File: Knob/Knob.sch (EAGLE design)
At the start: 17 parts, among them SW1 TopUp EC12PLRGBSDVBF-D, U2 ATTINY841

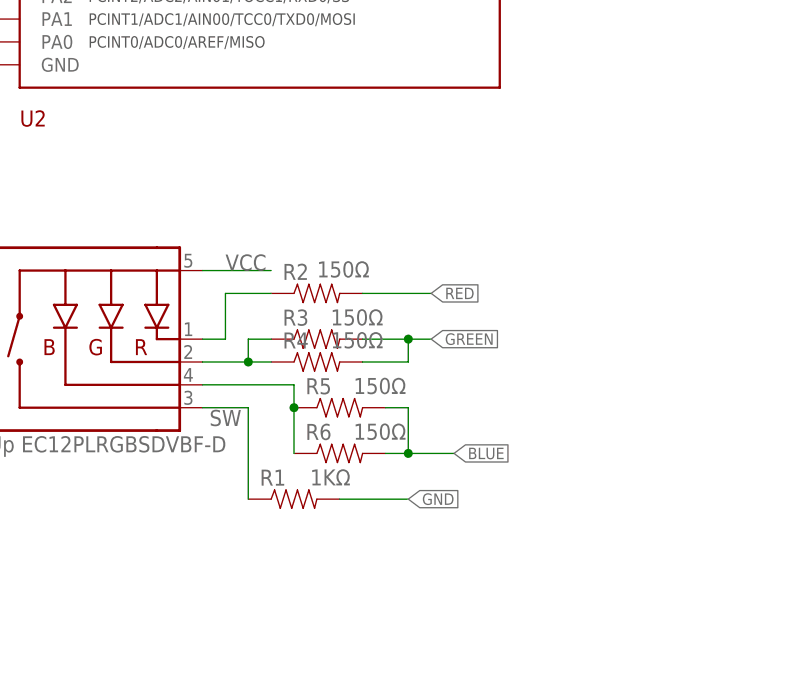
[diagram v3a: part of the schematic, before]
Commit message: Added parallel resistor on red channel for better white balance. Moved status LED to opposite side of the board next to logo Updated to new 0603 footprint.
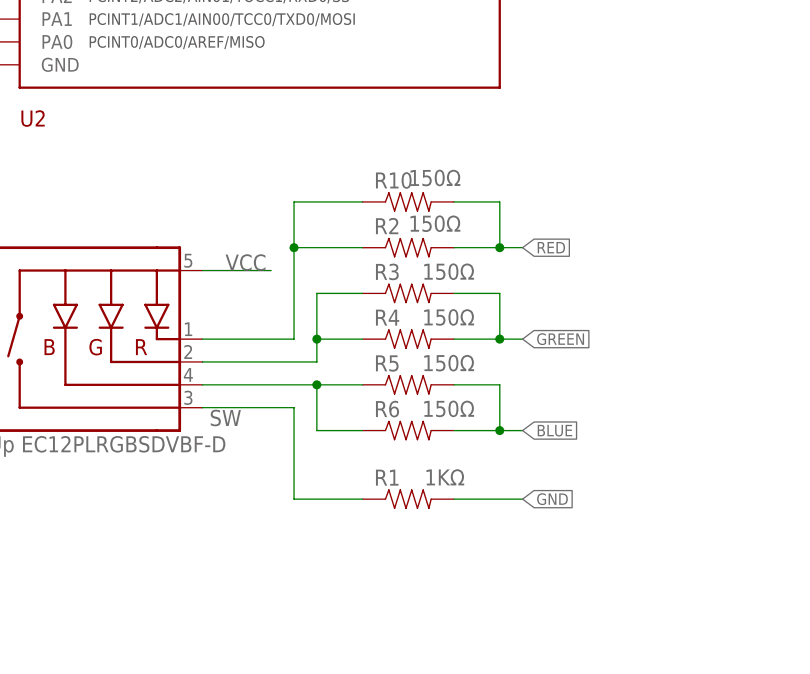
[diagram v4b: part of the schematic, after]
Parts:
- added R10: 150Ω, Modulo:RESISTOR-150Ω
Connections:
- net N$4: now also R10.1
- net RED: now also R10.2
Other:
- moved on the sheet: R1, R2, R3, R4, R5, R6
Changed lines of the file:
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@@
 <part name="R8" library="Modulo" deviceset="RESISTOR" device="-150Ω" value="150Ω"/>
 <part name="R9" library="Modulo" deviceset="RESISTOR" device="-150Ω" value="150Ω"/>
+<part name="R10" library="Modulo" deviceset="RESISTOR" device="-150Ω" value="150Ω"/>
 </parts>
 <sheets>
@@
 <attribute name="PARTNUM" x="63.5" y="73.66" size="1.778" layer="96" display="off"/>
 </instance>
-<instance part="R2" gate="G$1" x="91.44" y="78.74" smashed="yes">
-<attribute name="NAME" x="87.63" y="80.2386" size="1.778" layer="95"/>
-<attribute name="VALUE" x="91.44" y="80.518" size="1.778" layer="96"/>
-</instance>
-<instance part="R3" gate="G$1" x="91.44" y="73.66" smashed="yes">
-<attribute name="NAME" x="87.63" y="75.1586" size="1.778" layer="95"/>
-<attribute name="VALUE" x="92.964" y="75.184" size="1.778" layer="96"/>
-</instance>
-<instance part="R6" gate="G$1" x="93.98" y="60.96" smashed="yes">
-<attribute name="NAME" x="90.17" y="62.4586" size="1.778" layer="95"/>
-<attribute name="VALUE" x="95.504" y="62.484" size="1.778" layer="96"/>
-</instance>
-<instance part="R1" gate="G$1" x="88.9" y="55.88" smashed="yes">
-<attribute name="NAME" x="85.09" y="57.3786" size="1.778" layer="95"/>
-<attribute name="VALUE" x="90.678" y="57.404" size="1.778" layer="96"/>
+<instance part="R2" gate="G$1" x="101.6" y="83.82" smashed="yes">
+<attribute name="NAME" x="97.79" y="85.3186" size="1.778" layer="95"/>
+<attribute name="VALUE" x="101.6" y="85.598" size="1.778" layer="96"/>
+</instance>
+<instance part="R3" gate="G$1" x="101.6" y="78.74" smashed="yes">
+<attribute name="NAME" x="97.79" y="80.2386" size="1.778" layer="95"/>
+<attribute name="VALUE" x="103.124" y="80.264" size="1.778" layer="96"/>
+</instance>
+<instance part="R6" gate="G$1" x="101.6" y="63.5" smashed="yes">
+<attribute name="NAME" x="97.79" y="64.9986" size="1.778" layer="95"/>
+<attribute name="VALUE" x="103.124" y="65.024" size="1.778" layer="96"/>
+</instance>
+<instance part="R1" gate="G$1" x="101.6" y="55.88" smashed="yes">
+<attribute name="NAME" x="97.79" y="57.3786" size="1.778" layer="95"/>
+<attribute name="VALUE" x="103.378" y="57.404" size="1.778" layer="96"/>
 </instance>
 <instance part="FRAME1" gate="G$1" x="0" y="0">
@@
 <instance part="F1" gate="G$1" x="165.1" y="45.72"/>
 <instance part="F2" gate="G$1" x="190.5" y="45.72"/>
-<instance part="R5" gate="G$1" x="93.98" y="66.04" smashed="yes">
-<attribute name="NAME" x="90.17" y="67.5386" size="1.778" layer="95"/>
-<attribute name="VALUE" x="95.504" y="67.564" size="1.778" layer="96"/>
-</instance>
-<instance part="R4" gate="G$1" x="91.44" y="71.12" smashed="yes">
-<attribute name="NAME" x="87.63" y="72.6186" size="1.778" layer="95"/>
-<attribute name="VALUE" x="92.964" y="72.644" size="1.778" layer="96"/>
+<instance part="R5" gate="G$1" x="101.6" y="68.58" smashed="yes">
+<attribute name="NAME" x="97.79" y="70.0786" size="1.778" layer="95"/>
+<attribute name="VALUE" x="103.124" y="70.104" size="1.778" layer="96"/>
+</instance>
+<instance part="R4" gate="G$1" x="101.6" y="73.66" smashed="yes">
+<attribute name="NAME" x="97.79" y="75.1586" size="1.778" layer="95"/>
+<attribute name="VALUE" x="103.124" y="75.184" size="1.778" layer="96"/>
 </instance>
 <instance part="CAP1" gate="G$1" x="182.88" y="109.22">
@@
 <instance part="R8" gate="G$1" x="101.6" y="175.26"/>
 <instance part="R9" gate="G$1" x="45.72" y="175.26"/>
+<instance part="R10" gate="G$1" x="101.6" y="88.9" smashed="yes">
+<attribute name="NAME" x="97.79" y="90.3986" size="1.778" layer="95"/>
+<attribute name="VALUE" x="101.6" y="90.678" size="1.778" layer="96"/>
+</instance>
 </instances>
 <busses>
@@
 <segment>
 <pinref part="R1" gate="G$1" pin="2"/>
-<wire x1="93.98" y1="55.88" x2="101.6" y2="55.88" width="0.1524" layer="91"/>
-<label x="101.6" y="55.88" size="1.27" layer="95" xref="yes"/>
+<wire x1="106.68" y1="55.88" x2="114.3" y2="55.88" width="0.1524" layer="91"/>
+<label x="114.3" y="55.88" size="1.27" layer="95" xref="yes"/>
 </segment>
 <segment>
@@
 <label x="79.502" y="64.008" size="1.778" layer="95"/>
 <pinref part="R1" gate="G$1" pin="1"/>
-<wire x1="83.82" y1="55.88" x2="83.82" y2="66.04" width="0.1524" layer="91"/>
-<wire x1="83.82" y1="66.04" x2="78.74" y2="66.04" width="0.1524" layer="91"/>
+<wire x1="96.52" y1="55.88" x2="88.9" y2="55.88" width="0.1524" layer="91"/>
+<wire x1="88.9" y1="55.88" x2="88.9" y2="66.04" width="0.1524" layer="91"/>
+<wire x1="88.9" y1="66.04" x2="78.74" y2="66.04" width="0.1524" layer="91"/>
 </segment>
 <segment>
@@
 <pinref part="R2" gate="G$1" pin="1"/>
 <pinref part="SW1" gate="G$1" pin="-R"/>
-<wire x1="86.36" y1="78.74" x2="81.28" y2="78.74" width="0.1524" layer="91"/>
-<wire x1="81.28" y1="78.74" x2="81.28" y2="73.66" width="0.1524" layer="91"/>
-<wire x1="81.28" y1="73.66" x2="78.74" y2="73.66" width="0.1524" layer="91"/>
+<wire x1="96.52" y1="83.82" x2="88.9" y2="83.82" width="0.1524" layer="91"/>
+<wire x1="88.9" y1="83.82" x2="88.9" y2="73.66" width="0.1524" layer="91"/>
+<wire x1="88.9" y1="73.66" x2="78.74" y2="73.66" width="0.1524" layer="91"/>
+<wire x1="88.9" y1="83.82" x2="88.9" y2="88.9" width="0.1524" layer="91"/>
+<pinref part="R10" gate="G$1" pin="1"/>
+<wire x1="88.9" y1="88.9" x2="96.52" y2="88.9" width="0.1524" layer="91"/>
+<junction x="88.9" y="83.82"/>
 </segment>
 </net>
@@
 <pinref part="SW1" gate="G$1" pin="-G"/>
 <pinref part="R3" gate="G$1" pin="1"/>
-<wire x1="78.74" y1="71.12" x2="83.82" y2="71.12" width="0.1524" layer="91"/>
-<wire x1="83.82" y1="71.12" x2="83.82" y2="73.66" width="0.1524" layer="91"/>
-<wire x1="83.82" y1="73.66" x2="86.36" y2="73.66" width="0.1524" layer="91"/>
+<wire x1="78.74" y1="71.12" x2="91.44" y2="71.12" width="0.1524" layer="91"/>
+<wire x1="91.44" y1="71.12" x2="91.44" y2="73.66" width="0.1524" layer="91"/>
+<wire x1="91.44" y1="73.66" x2="91.44" y2="78.74" width="0.1524" layer="91"/>
+<wire x1="91.44" y1="78.74" x2="96.52" y2="78.74" width="0.1524" layer="91"/>
 <pinref part="R4" gate="G$1" pin="1"/>
-<wire x1="83.82" y1="71.12" x2="86.36" y2="71.12" width="0.1524" layer="91"/>
-<junction x="83.82" y="71.12"/>
+<wire x1="91.44" y1="73.66" x2="96.52" y2="73.66" width="0.1524" layer="91"/>
+<junction x="91.44" y="73.66"/>
 </segment>
 </net>
@@
 <pinref part="SW1" gate="G$1" pin="-B"/>
 <pinref part="R6" gate="G$1" pin="1"/>
-<wire x1="78.74" y1="68.58" x2="88.9" y2="68.58" width="0.1524" layer="91"/>
-<wire x1="88.9" y1="68.58" x2="88.9" y2="66.04" width="0.1524" layer="91"/>
+<wire x1="78.74" y1="68.58" x2="91.44" y2="68.58" width="0.1524" layer="91"/>
 <pinref part="R5" gate="G$1" pin="1"/>
-<wire x1="88.9" y1="66.04" x2="88.9" y2="60.96" width="0.1524" layer="91"/>
-<junction x="88.9" y="66.04"/>
+<wire x1="96.52" y1="68.58" x2="91.44" y2="68.58" width="0.1524" layer="91"/>
+<wire x1="91.44" y1="68.58" x2="91.44" y2="63.5" width="0.1524" layer="91"/>
+<wire x1="91.44" y1="63.5" x2="96.52" y2="63.5" width="0.1524" layer="91"/>
+<junction x="91.44" y="68.58"/>
 </segment>
 </net>
@@
 <segment>
 <pinref part="R2" gate="G$1" pin="2"/>
-<wire x1="96.52" y1="78.74" x2="104.14" y2="78.74" width="0.1524" layer="91"/>
-<label x="104.14" y="78.74" size="1.27" layer="95" xref="yes"/>
+<wire x1="106.68" y1="83.82" x2="111.76" y2="83.82" width="0.1524" layer="91"/>
+<label x="114.3" y="83.82" size="1.27" layer="95" xref="yes"/>
+<pinref part="R10" gate="G$1" pin="2"/>
+<wire x1="111.76" y1="83.82" x2="114.3" y2="83.82" width="0.1524" layer="91"/>
+<wire x1="106.68" y1="88.9" x2="111.76" y2="88.9" width="0.1524" layer="91"/>
+<wire x1="111.76" y1="88.9" x2="111.76" y2="83.82" width="0.1524" layer="91"/>
+<junction x="111.76" y="83.82"/>
 </segment>
 <segment>
@@
 <segment>
 <pinref part="R3" gate="G$1" pin="2"/>
-<wire x1="96.52" y1="73.66" x2="101.6" y2="73.66" width="0.1524" layer="91"/>
-<label x="104.14" y="73.66" size="1.27" layer="95" xref="yes"/>
+<wire x1="106.68" y1="78.74" x2="111.76" y2="78.74" width="0.1524" layer="91"/>
+<label x="114.3" y="73.66" size="1.27" layer="95" xref="yes"/>
 <pinref part="R4" gate="G$1" pin="2"/>
-<wire x1="101.6" y1="73.66" x2="104.14" y2="73.66" width="0.1524" layer="91"/>
-<wire x1="96.52" y1="71.12" x2="101.6" y2="71.12" width="0.1524" layer="91"/>
-<wire x1="101.6" y1="71.12" x2="101.6" y2="73.66" width="0.1524" layer="91"/>
-<junction x="101.6" y="73.66"/>
+<wire x1="106.68" y1="73.66" x2="111.76" y2="73.66" width="0.1524" layer="91"/>
+<wire x1="111.76" y1="73.66" x2="111.76" y2="78.74" width="0.1524" layer="91"/>
+<wire x1="111.76" y1="73.66" x2="114.3" y2="73.66" width="0.1524" layer="91"/>
+<junction x="111.76" y="73.66"/>
 </segment>
 <segment>
@@
 <segment>
 <pinref part="R6" gate="G$1" pin="2"/>
-<wire x1="99.06" y1="60.96" x2="101.6" y2="60.96" width="0.1524" layer="91"/>
-<label x="106.68" y="60.96" size="1.27" layer="95" xref="yes"/>
-<wire x1="101.6" y1="60.96" x2="106.68" y2="60.96" width="0.1524" layer="91"/>
-<wire x1="101.6" y1="60.96" x2="101.6" y2="66.04" width="0.1524" layer="91"/>
+<wire x1="106.68" y1="63.5" x2="111.76" y2="63.5" width="0.1524" layer="91"/>
+<label x="114.3" y="63.5" size="1.27" layer="95" xref="yes"/>
+<wire x1="111.76" y1="63.5" x2="114.3" y2="63.5" width="0.1524" layer="91"/>
+<wire x1="111.76" y1="63.5" x2="111.76" y2="68.58" width="0.1524" layer="91"/>
 <pinref part="R5" gate="G$1" pin="2"/>
-<wire x1="101.6" y1="66.04" x2="99.06" y2="66.04" width="0.1524" layer="91"/>
-<junction x="101.6" y="60.96"/>
-</segment>
-<segment>
+<wire x1="111.76" y1="68.58" x2="106.68" y2="68.58" width="0.1524" layer="91"/>
+<junction x="111.76" y="63.5"/>
+</segment>
+<segment>

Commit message: Various small tweaks based on testing and feedback from manufacturer.
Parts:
- R8, R9: value 150Ω -> 0Ω; device Modulo:RESISTOR-150Ω -> Modulo:RESISTOR-0Ω
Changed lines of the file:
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@@
 </part>
 <part name="U2" library="Modulo" deviceset="ATTINY841" device=""/>
-<part name="R8" library="Modulo" deviceset="RESISTOR" device="-150Ω" value="150Ω"/>
-<part name="R9" library="Modulo" deviceset="RESISTOR" device="-150Ω" value="150Ω"/>
+<part name="R8" library="Modulo" deviceset="RESISTOR" device="-0Ω" value="0Ω"/>
+<part name="R9" library="Modulo" deviceset="RESISTOR" device="-0Ω" value="0Ω"/>
 <part name="R10" library="Modulo" deviceset="RESISTOR" device="-150Ω" value="150Ω"/>
 </parts>

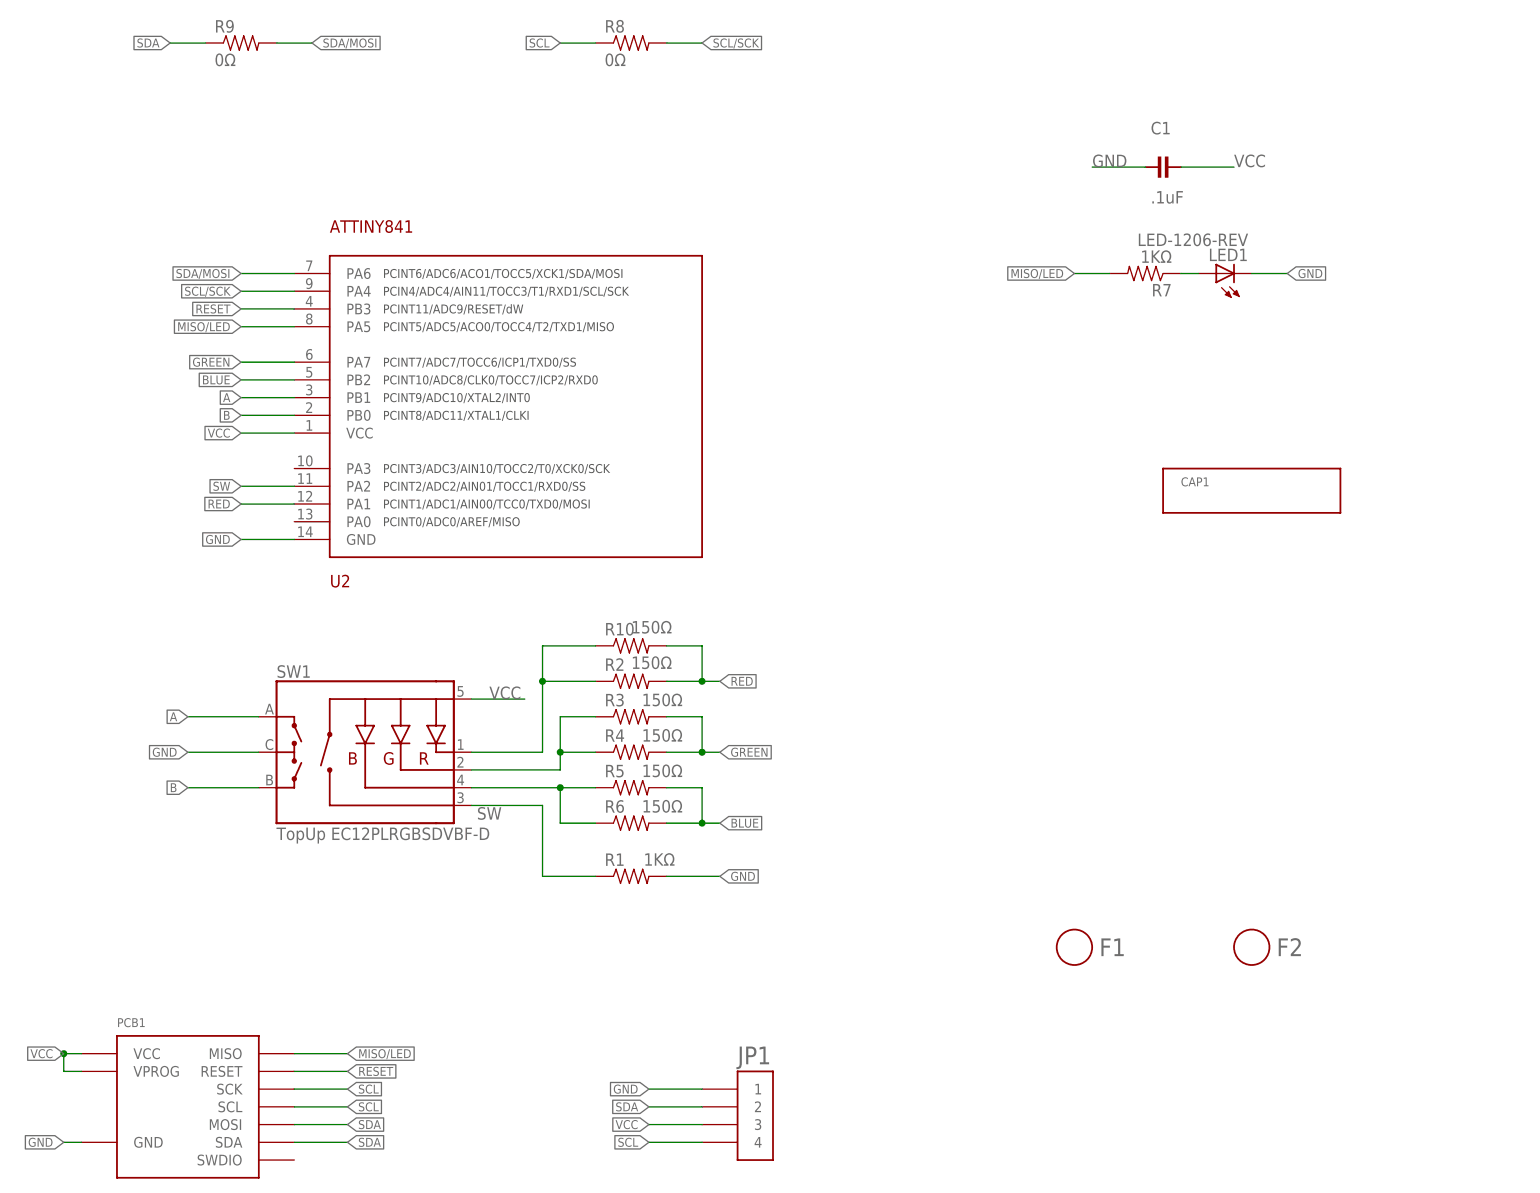
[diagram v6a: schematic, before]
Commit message: Added unique board prefixes to part numbers due to CM requirements
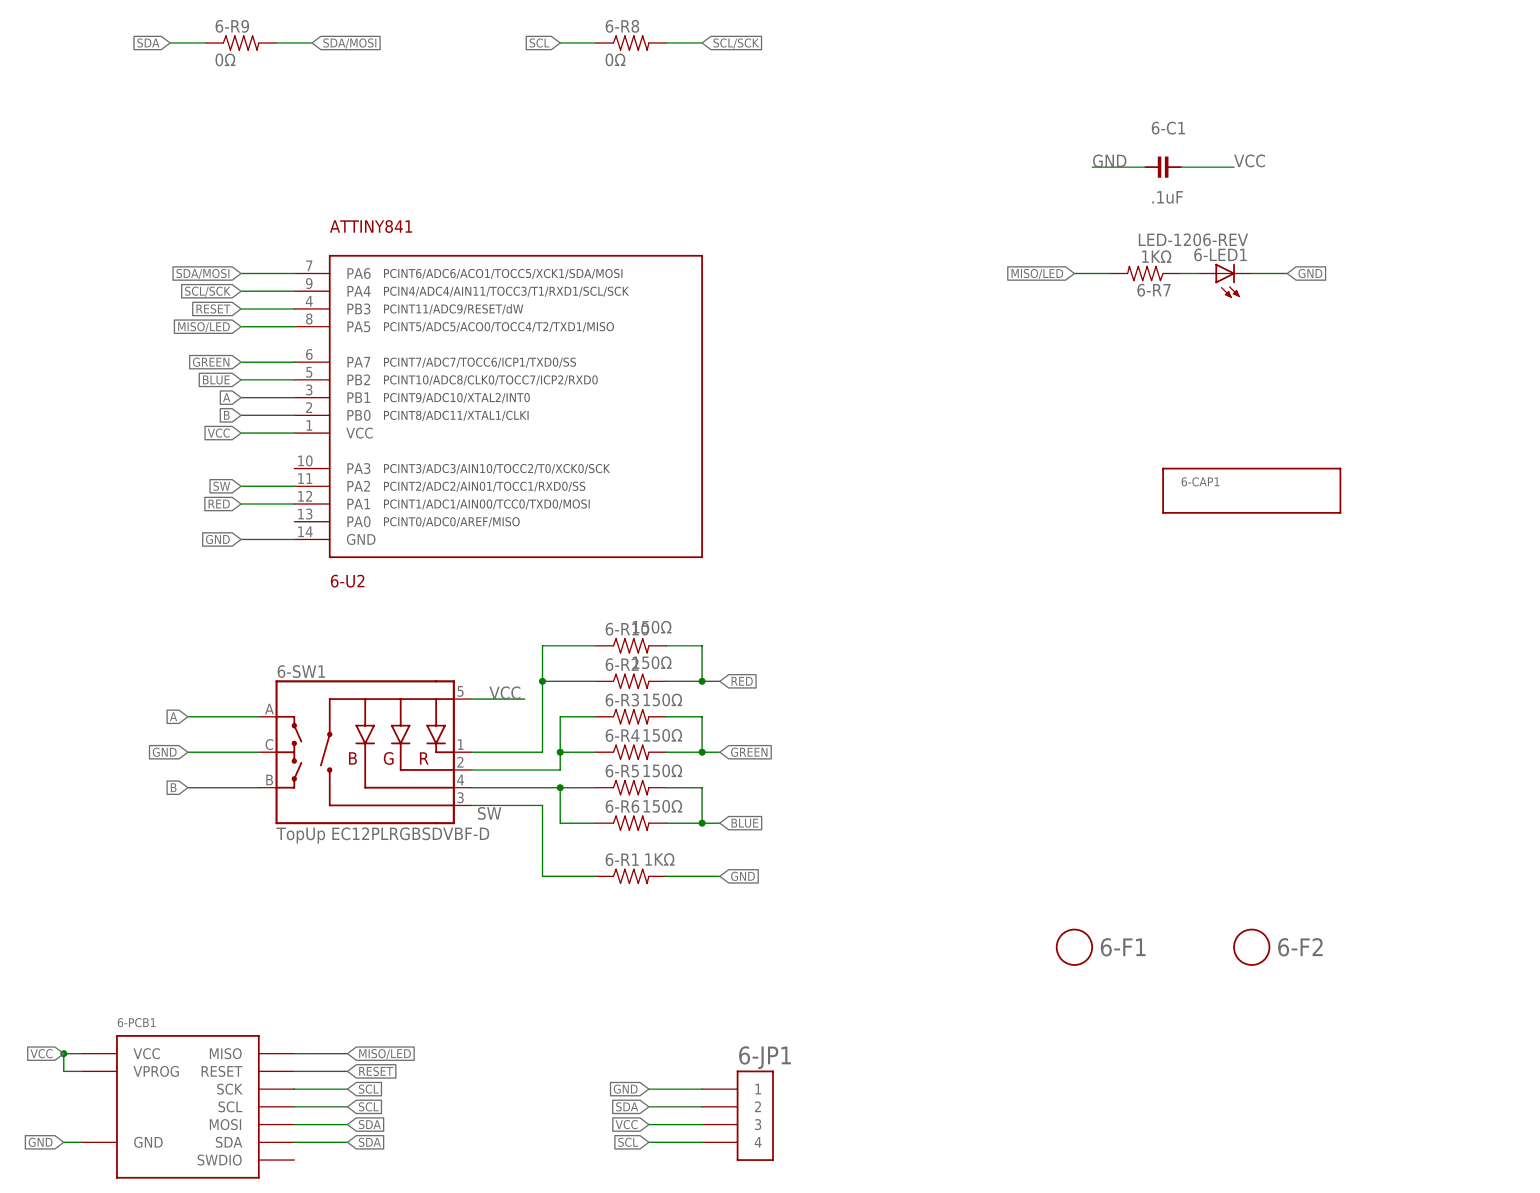
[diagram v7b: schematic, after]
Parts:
- renumbered C1 to 6-C1, F1 to 6-F1, F2 to 6-F2, JP1 to 6-JP1, LED1 to 6-LED1, PCB1 to 6-PCB1, R1 to 6-R1, R10 to 6-R10, R2 to 6-R2, R3 to 6-R3, R4 to 6-R4, R5 to 6-R5, R6 to 6-R6, R7 to 6-R7, R8 to 6-R8, R9 to 6-R9, SW1 to 6-SW1, U2 to 6-U2
